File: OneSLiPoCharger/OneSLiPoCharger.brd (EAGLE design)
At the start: 86.4 x 52.1 mm, 58 parts, among them IC1 LM358N, Q1 BUZ10

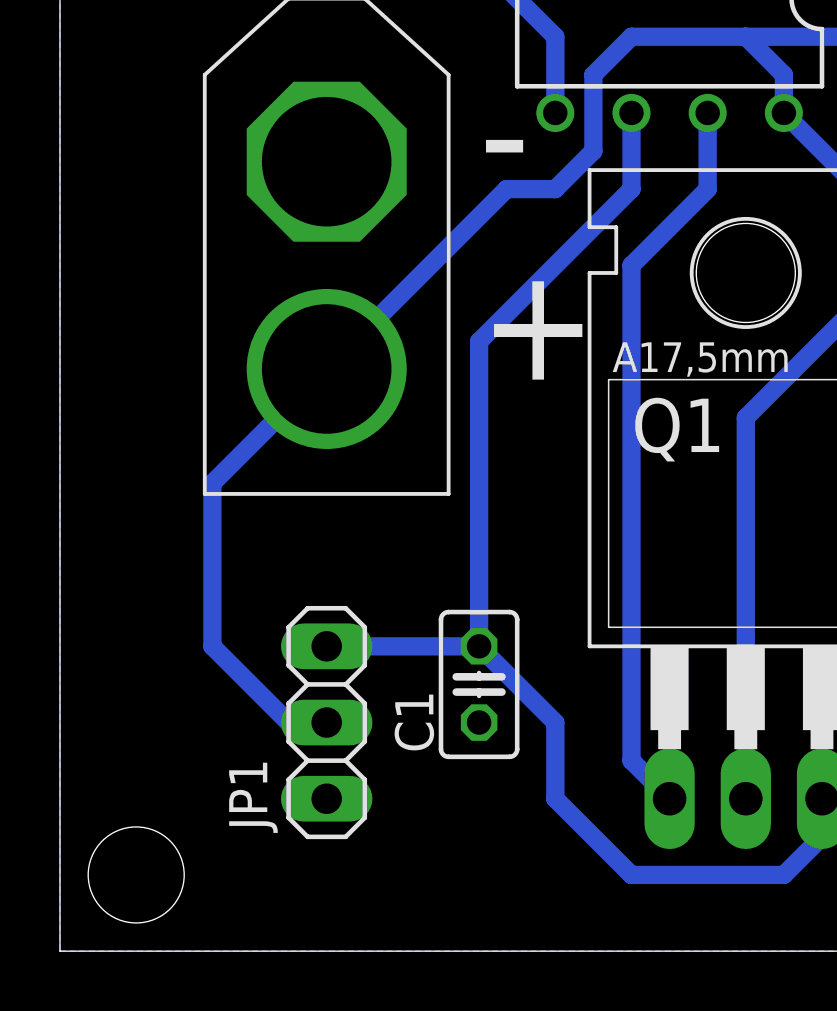
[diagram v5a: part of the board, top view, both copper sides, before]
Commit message: Rotate smoothing cap to allow for horizontal electrolitic if needed.
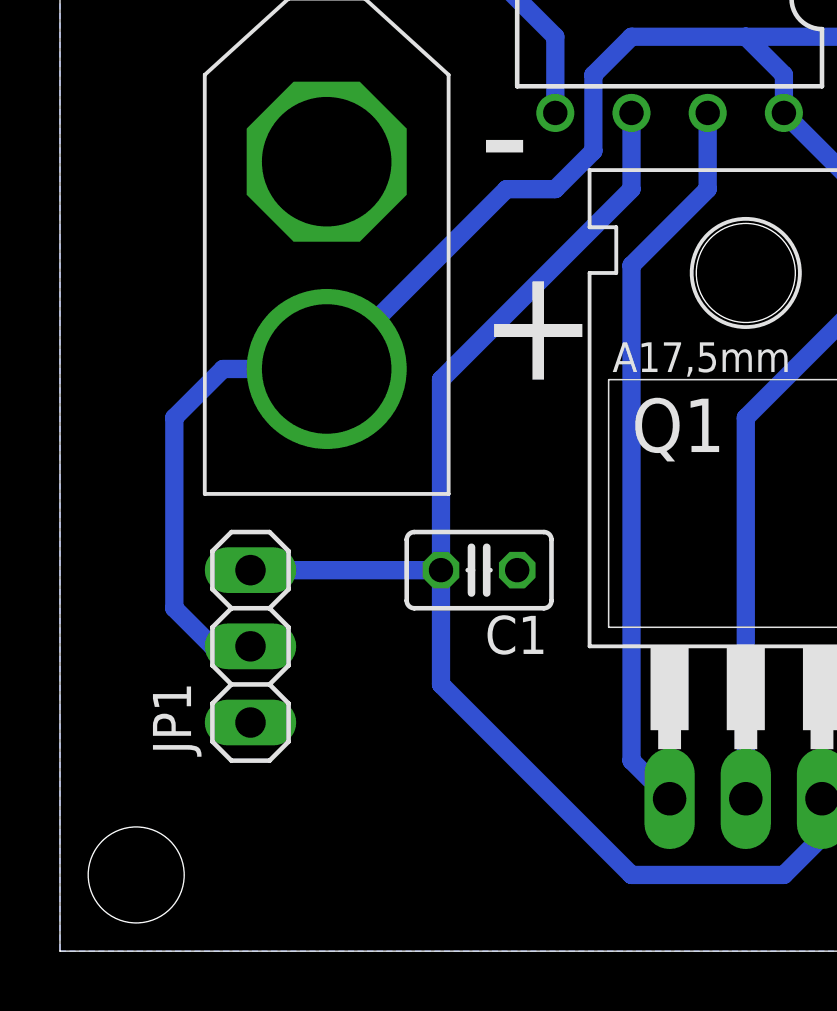
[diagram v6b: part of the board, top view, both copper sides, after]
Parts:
- moved C1 3.81 mm to (14.0, 12.7), turned to 180 degrees
- moved JP1 3.59 mm to (6.35, 10.2)
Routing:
- net +5V: track 287.9 -> 290.2 mm
- net VCC: track 104.3 -> 103.8 mm
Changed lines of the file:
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@@
 </autorouter>
 <elements>
-<element name="C1" library="rcl" package="C025-025X050" value="" x="13.97" y="8.89" rot="R90"/>
+<element name="C1" library="rcl" package="C025-025X050" value="" x="13.97" y="12.7" rot="R180"/>
 <element name="C2" library="rcl" package="C0805" value="4.7uF" x="43.18" y="36.83" smashed="yes" rot="MR90">
 <attribute name="NAME" x="40.64" y="35.56" size="1.27" layer="26" rot="MR90"/>
@@
 <attribute name="NAME" x="69.85" y="15.24" size="1.27" layer="26" rot="MR90"/>
 </element>
-<element name="JP1" library="pinhead" package="1X03" value="" x="8.89" y="7.62" smashed="yes" rot="R270">
-<attribute name="NAME" x="5.6388" y="6.4262" size="1.27" layer="25" ratio="10" rot="R270"/>
-<attribute name="VALUE" x="5.715" y="11.43" size="1.27" layer="27" rot="R270"/>
+<element name="JP1" library="pinhead" package="1X03" value="" x="6.35" y="10.16" smashed="yes" rot="R270">
+<attribute name="NAME" x="3.0988" y="8.9662" size="1.27" layer="25" ratio="10" rot="R270"/>
+<attribute name="VALUE" x="3.175" y="13.97" size="1.27" layer="27" rot="R270"/>
 </element>
 <element name="DRILEGEND" library="drilegend" package="DRILEGEND" value="" x="-17.78" y="-9.8044"/>
@@
 <wire x1="26.67" y1="25.4" x2="24.13" y2="27.94" width="0.6096" layer="16"/>
 <contactref element="JP1" pad="2"/>
-<wire x1="8.89" y1="19.4056" x2="5.08" y2="15.5956" width="0.6096" layer="16"/>
-<wire x1="5.08" y1="15.5956" x2="5.08" y2="10.16" width="0.6096" layer="16"/>
-<wire x1="5.08" y1="10.16" x2="7.62" y2="7.62" width="0.6096" layer="16"/>
-<wire x1="7.62" y1="7.62" x2="8.89" y2="7.62" width="0.6096" layer="16"/>
 <wire x1="19.05" y1="30.48" x2="17.78" y2="29.21" width="0.6096" layer="16"/>
 <wire x1="17.78" y1="29.21" x2="17.78" y2="26.67" width="0.6096" layer="16"/>
@@
 <wire x1="22.86" y1="40.64" x2="31.75" y2="40.64" width="0.6096" layer="16"/>
 <wire x1="31.75" y1="40.64" x2="34.29" y2="43.18" width="0.6096" layer="16"/>
+<wire x1="8.89" y1="19.4056" x2="5.4356" y2="19.4056" width="0.6096" layer="16"/>
+<wire x1="5.4356" y1="19.4056" x2="3.81" y2="17.78" width="0.6096" layer="16"/>
+<wire x1="3.81" y1="17.78" x2="3.81" y2="11.43" width="0.6096" layer="16"/>
+<wire x1="3.81" y1="11.43" x2="5.08" y2="10.16" width="0.6096" layer="16"/>
+<wire x1="5.08" y1="10.16" x2="6.35" y2="10.16" width="0.6096" layer="16"/>
 </signal>
 <signal name="GND">
@@
 <wire x1="45.72" y1="26.67" x2="48.26" y2="26.67" width="0.6096" layer="16"/>
 <contactref element="JP1" pad="1"/>
-<wire x1="8.89" y1="10.16" x2="13.97" y2="10.16" width="0.6096" layer="16"/>
-<wire x1="13.97" y1="10.16" x2="16.51" y2="7.62" width="0.6096" layer="16"/>
-<wire x1="16.51" y1="7.62" x2="16.51" y2="5.08" width="0.6096" layer="16"/>
-<wire x1="16.51" y1="5.08" x2="19.05" y2="2.54" width="0.6096" layer="16"/>
 <wire x1="19.05" y1="2.54" x2="24.13" y2="2.54" width="0.6096" layer="16"/>
 <wire x1="24.13" y1="2.54" x2="25.4" y2="3.81" width="0.6096" layer="16"/>
@@
 <contactref element="IC1" pad="6"/>
 <wire x1="19.05" y1="27.94" x2="19.05" y2="25.4" width="0.6096" layer="16"/>
-<wire x1="19.05" y1="25.4" x2="13.97" y2="20.32" width="0.6096" layer="16"/>
-<wire x1="13.97" y1="20.32" x2="13.97" y2="10.16" width="0.6096" layer="16"/>
+<wire x1="19.05" y1="25.4" x2="12.7" y2="19.05" width="0.6096" layer="16"/>
 <wire x1="34.29" y1="8.89" x2="34.29" y2="15.24" width="0.6096" layer="16"/>
 <wire x1="34.29" y1="15.24" x2="45.72" y2="26.67" width="0.6096" layer="16"/>
+<wire x1="12.7" y1="12.7" x2="6.35" y2="12.7" width="0.6096" layer="16"/>
+<wire x1="12.7" y1="12.7" x2="12.7" y2="19.05" width="0.6096" layer="16"/>
+<wire x1="12.7" y1="12.7" x2="12.7" y2="8.89" width="0.6096" layer="16"/>
+<wire x1="12.7" y1="8.89" x2="19.05" y2="2.54" width="0.6096" layer="16"/>
 </signal>
 <signal name="N$10">
